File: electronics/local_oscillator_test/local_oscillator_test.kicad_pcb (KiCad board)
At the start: 2 copper layers, 0 parts

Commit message: Import works
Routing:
- removed copper zone on F.Cu, net (none)
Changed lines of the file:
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@@
     (visible_elements FFFFFF7F)
     (pcbplotparams
-      (layerselection 0x010fc_ffffffff)
+      (layerselection 0x00000_7fffffff)
       (usegerberextensions false)
       (usegerberattributes false)
@@
       (psnegative false)
       (psa4output false)
-      (plotreference true)
-      (plotvalue true)
+      (plotreference false)
+      (plotvalue false)
       (plotinvisibletext false)
       (padsonsilk false)
       (subtractmaskfromsilk false)
-      (outputformat 1)
+      (outputformat 4)
       (mirror false)
-      (drillshape 1)
+      (drillshape 0)
       (scaleselection 1)
       (outputdirectory ""))
@@
     (uvia_drill 0.1)
   )
-  (zone (net 0) (net_name "") (layer F.Cu) (hatch edge 0.508)
-    (connect_pads (clearance 0.508))
-    (min_thickness 0.254)
-    (fill yes (arc_segments 16) (thermal_gap 0.508) (thermal_bridge_width 0.508))
-    (polygon
-      (pts
-        (xy 100 45) (xy 110 45) (xy 110 55) (xy 100 55)
-      )
-    )
-  )
 )

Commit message: Modelled reference oscillator, gprMax impulse model is looking fine
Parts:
- added C1: 1pF, 0402, F.Cu at (18.4, 20.0)
- added U1: CE3520K3, 0xDBFB7:4-Micro-X, F.Cu at (22.4, 20.0)
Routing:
- net (no net): track 0.00 -> 55.0 mm
- net GND: track 0.00 -> 2.75 mm
- net /OSC1: track 0.00 -> 2.75 mm
- net /GATE: track 0.00 -> 2.75 mm
- added copper zone on F.Cu, net /GATE
- added copper zone on F.Cu, net /OSC1
- added copper zone on F.Cu, net GND
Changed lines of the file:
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@@
     (thickness 1.6)
     (drawings 0)
-    (tracks 0)
+    (tracks 8)
     (zones 0)
-    (modules 0)
-    (nets 1)
+    (modules 2)
+    (nets 4)
   )
   (page A4)
@@
     (last_trace_width 0.25)
     (trace_clearance 0.2)
-    (zone_clearance 0.508)
+    (zone_clearance 0)
     (zone_45_only no)
     (trace_min 0.2)
@@
     (pad_drill 0.762)
     (pad_to_mask_clearance 0.2)
-    (aux_axis_origin 0 0)
-    (visible_elements FFFFFF7F)
+    (aux_axis_origin 22.5 25)
+    (grid_origin 22.5 25)
+    (visible_elements FEFFFF7F)
     (pcbplotparams
       (layerselection 0x00000_7fffffff)
@@
   )
   (net 0 "")
+  (net 1 /OSC1)
+  (net 2 GND)
+  (net 3 /GATE)
   (net_class Default "This is the default net class."
     (clearance 0.2)
@@
     (uvia_dia 0.3)
     (uvia_drill 0.1)
+    (add_net /GATE)
+    (add_net /OSC1)
+    (add_net GND)
+  )
+  (module 0402 (layer F.Cu)
+    (at 18.35 20 90)
+    (descr "GENERIC 1005 (0402) PACKAGE")
+    (tags "GENERIC 1005 (0402) PACKAGE")
+    (attr smd)
+    (fp_text reference C1 (at 0 -1.27 90) (layer F.SilkS)
+      (effects (font (size 0.6096 0.6096) (thickness 0.127)))
+    )
+    (fp_text value 1pF (at 0 1.27 90) (layer F.SilkS)
+      (effects (font (size 0.6096 0.6096) (thickness 0.127)))
+    )
+    (fp_line (start -0.55372 0.3048) (end -0.254 0.3048) (layer Dwgs.User) (width 0.06604))
+    (fp_line (start -0.254 0.3048) (end -0.254 -0.3048) (layer Dwgs.User) (width 0.06604))
+    (fp_line (start -0.55372 -0.3048) (end -0.254 -0.3048) (layer Dwgs.User) (width 0.06604))
+    (fp_line (start -0.55372 0.3048) (end -0.55372 -0.3048) (layer Dwgs.User) (width 0.06604))
+    (fp_line (start 0.25654 0.3048) (end 0.5588 0.3048) (layer Dwgs.User) (width 0.06604))
+    (fp_line (start 0.5588 0.3048) (end 0.5588 -0.3048) (layer Dwgs.User) (width 0.06604))
+    (fp_line (start 0.25654 -0.3048) (end 0.5588 -0.3048) (layer Dwgs.User) (width 0.06604))
+    (fp_line (start 0.25654 0.3048) (end 0.25654 -0.3048) (layer Dwgs.User) (width 0.06604))
+    (fp_line (start -0.19812 0.29972) (end 0.19812 0.29972) (layer F.SilkS) (width 0.06604))
+    (fp_line (start 0.19812 0.29972) (end 0.19812 -0.29972) (layer F.SilkS) (width 0.06604))
+    (fp_line (start -0.19812 -0.29972) (end 0.19812 -0.29972) (layer F.SilkS) (width 0.06604))
+    (fp_line (start -0.19812 0.29972) (end -0.19812 -0.29972) (layer F.SilkS) (width 0.06604))
+    (fp_line (start -0.26924 -0.2286) (end 0.26924 -0.2286) (layer Dwgs.User) (width 0.1524))
+    (fp_line (start 0.26924 0.2286) (end -0.26924 0.2286) (layer Dwgs.User) (width 0.1524))
+    (fp_line (start -1.19888 -0.6477) (end 1.19888 -0.6477) (layer F.CrtYd) (width 0.0508))
+    (fp_line (start 1.19888 -0.6477) (end 1.19888 0.6477) (layer F.CrtYd) (width 0.0508))
+    (fp_line (start 1.19888 0.6477) (end -1.19888 0.6477) (layer F.CrtYd) (width 0.0508))
+    (fp_line (start -1.19888 0.6477) (end -1.19888 -0.6477) (layer F.CrtYd) (width 0.0508))
+    (pad 1 smd rect (at -0.57912 0 90) (size 0.84836 0.89916) (layers F.Cu F.Paste F.Mask)
+      (net 3 /GATE) (solder_mask_margin 0.1016))
+    (pad 2 smd rect (at 0.57912 0 90) (size 0.84836 0.89916) (layers F.Cu F.Paste F.Mask)
+      (net 1 /OSC1) (solder_mask_margin 0.1016))
+  )
+  (module 0xDBFB7:4-Micro-X (layer F.Cu)
+    (at 22.45 20 270)
+    (fp_text reference U1 (at 0 5.072 270) (layer F.SilkS)
+      (effects (font (size 1 1) (thickness 0.15)))
+    )
+    (fp_text value CE3520K3 (at 0 4.072 270) (layer F.Fab)
+      (effects (font (size 1 1) (thickness 0.15)))
+    )
+    (fp_text user Gate (at 1.4 -0.5 270) (layer Dwgs.User)
+      (effects (font (size 0.2 0.2) (thickness 0.05)))
+    )
+    (fp_text user Drain (at -1.3 -0.5 270) (layer Dwgs.User)
+      (effects (font (size 0.2 0.2) (thickness 0.05)))
+    )
+    (fp_text user Source (at -0.5 -1.3) (layer Dwgs.User)
+      (effects (font (size 0.2 0.2) (thickness 0.05)))
+    )
+    (fp_text user Source (at -0.5 1.4) (layer Dwgs.User)
+      (effects (font (size 0.2 0.2) (thickness 0.05)))
+    )
+    (fp_circle (center 0 0) (end 0.583095 0) (layer F.SilkS) (width 0.15))
+    (fp_circle (center 0.4 0) (end 0.5 0) (layer F.SilkS) (width 0.15))
+    (pad 2 smd rect (at -1.35 0) (size 0.65 1) (layers F.Cu F.Paste F.Mask)
+      (net 1 /OSC1))
+    (pad 1 smd rect (at 0 -1.35 270) (size 0.65 1) (layers F.Cu F.Paste F.Mask)
+      (net 2 GND))
+    (pad 4 smd rect (at 1.35 0 180) (size 0.65 1) (layers F.Cu F.Paste F.Mask)
+      (net 3 /GATE))
+    (pad 3 smd rect (at 0 1.35 90) (size 0.65 1) (layers F.Cu F.Paste F.Mask)
+      (net 2 GND))
+  )
+  (segment (start 27.5 27.5) (end 27.5 12.5) (width 0.25) (layer F.Cu) (net 0))
+  (segment (start 15 12.5) (end 15 27.5) (width 0.25) (layer F.Cu) (net 0))
+  (segment (start 15 27.5) (end 27.5 27.5) (width 0.25) (layer F.Cu) (net 0))
+  (segment (start 15 12.5) (end 27.25 12.5) (width 0.25) (layer F.Cu) (net 0))
+  (segment (start 27.25 12.5) (end 27.5 12.5) (width 0.25) (layer F.Cu) (net 0))
+  (segment (start 26.95 20) (end 24.2 20) (width 0.1) (layer F.Cu) (net 2))
+  (segment (start 22.45 22.5) (end 22.45 25.25) (width 0.1) (layer F.Cu) (net 3))
+  (segment (start 22.45 14.75) (end 22.45 17.5) (width 0.1) (layer F.Cu) (net 1))
+  (zone (net 3) (net_name /GATE) (layer F.Cu) (hatch edge 0.508)
+    (connect_pads yes (clearance 0.508))
+    (min_thickness 0.254)
+    (fill yes (arc_segments 16) (thermal_gap 0.508) (thermal_bridge_width 0.508))
+    (polygon
+      (pts
+        (xy 24.95 22.5) (xy 24.95 21) (xy 19.95 21) (xy 19.95 22.5)
+      )
+    )
+  )
+  (zone (net 1) (net_name /OSC1) (layer F.Cu) (hatch edge 0.508)
+    (connect_pads yes (clearance 0.508))
+    (min_thickness 0.254)
+    (fill yes (arc_segments 16) (thermal_gap 0.508) (thermal_bridge_width 0.508))
+    (polygon
+      (pts
+        (xy 24.95 19) (xy 24.95 17.5) (xy 19.95 17.5) (xy 19.95 19)
+      )
+    )
+  )
+  (zone (net 2) (net_name GND) (layer F.Cu) (hatch edge 0.508)
+    (connect_pads yes (clearance 0))
+    (min_thickness 0.254)
+    (fill yes (arc_segments 16) (thermal_gap 0) (thermal_bridge_width 0))
+    (polygon
+      (pts
+        (xy 19.95 19.75) (xy 24.95 19.75) (xy 24.95 20.25) (xy 19.95 20.25)
+      )
+    )
+  )
+  (zone (net 1) (net_name /OSC1) (layer F.Cu) (hatch edge 0.508)
+    (connect_pads yes (clearance 0))
+    (min_thickness 0.254)
+    (fill yes (arc_segments 16) (thermal_gap 0) (thermal_bridge_width 0))
+    (polygon
+      (pts
+        (xy 20.45 18) (xy 20.45 16.5) (xy 19.95 16.5) (xy 19.95 18)
+      )
+    )
+  )
+  (zone (net 1) (net_name /OSC1) (layer F.Cu) (hatch edge 0.508)
+    (connect_pads yes (clearance 0))
+    (min_thickness 0.254)
+    (fill yes (arc_segments 16) (thermal_gap 0) (thermal_bridge_width 0))
+    (polygon
+      (pts
+        (xy 20.45 16.5) (xy 20.45 17.25) (xy 17.95 17.25) (xy 17.95 16.5)
+      )
+    )
+  )
+  (zone (net 1) (net_name /OSC1) (layer F.Cu) (hatch edge 0.508)
+    (connect_pads yes (clearance 0))
+    (min_thickness 0.254)
+    (fill yes (arc_segments 16) (thermal_gap 0) (thermal_bridge_width 0))
+    (polygon
+      (pts
+        (xy 17.95 16.5) (xy 17.95 19.5) (xy 18.7 19.5) (xy 18.7 16.5)
+      )
+    )
+  )
+  (zone (net 3) (net_name /GATE) (layer F.Cu) (hatch edge 0.508)
+    (connect_pads yes (clearance 0))
+    (min_thickness 0.254)
+    (fill yes (arc_segments 16) (thermal_gap 0) (thermal_bridge_width 0))
+    (polygon
+      (pts
+        (xy 20.45 22) (xy 20.45 23.5) (xy 19.95 23.5) (xy 19.95 22)
+      )
+    )
+  )
+  (zone (net 3) (net_name /GATE) (layer F.Cu) (hatch edge 0.508)
+    (connect_pads yes (clearance 0))
+    (min_thickness 0.254)
+    (fill yes (arc_segments 16) (thermal_gap 0) (thermal_bridge_width 0))
+    (polygon
+      (pts
+        (xy 20.45 23.5) (xy 17.95 23.5) (xy 17.95 20.5) (xy 18.7 20.5) (xy 18.7 22.75)
+        (xy 20.45 22.75)
+      )
+    )
   )
 )

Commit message: Something resembling an impulse
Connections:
- C1 pad 2: /OSC1 -> /GATE
- U1 pad 2: /OSC1 -> /GATE
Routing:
- net (no net): track 55.0 -> 1.00 mm
- net /GATE: track 2.75 -> 3.91 mm
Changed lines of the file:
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@@
       (net 3 /GATE) (solder_mask_margin 0.1016))
     (pad 2 smd rect (at 0.57912 0 90) (size 0.84836 0.89916) (layers F.Cu F.Paste F.Mask)
-      (net 1 /OSC1) (solder_mask_margin 0.1016))
+      (net 3 /GATE) (solder_mask_margin 0.1016))
   )
   (module 0xDBFB7:4-Micro-X (layer F.Cu)
@@
     (fp_circle (center 0.4 0) (end 0.5 0) (layer F.SilkS) (width 0.15))
     (pad 2 smd rect (at -1.35 0) (size 0.65 1) (layers F.Cu F.Paste F.Mask)
-      (net 1 /OSC1))
+      (net 3 /GATE))
     (pad 1 smd rect (at 0 -1.35 270) (size 0.65 1) (layers F.Cu F.Paste F.Mask)
       (net 2 GND))
@@
       (net 2 GND))
   )
-  (segment (start 27.5 27.5) (end 27.5 12.5) (width 0.25) (layer F.Cu) (net 0))
-  (segment (start 15 12.5) (end 15 27.5) (width 0.25) (layer F.Cu) (net 0))
-  (segment (start 15 27.5) (end 27.5 27.5) (width 0.25) (layer F.Cu) (net 0))
-  (segment (start 15 12.5) (end 27.25 12.5) (width 0.25) (layer F.Cu) (net 0))
-  (segment (start 27.25 12.5) (end 27.5 12.5) (width 0.25) (layer F.Cu) (net 0))
+  (segment (start 15 12.75) (end 15 12.5) (width 0.05) (layer F.Cu) (net 0))
+  (segment (start 15 12.5) (end 15.25 12.5) (width 0.05) (layer F.Cu) (net 0))
+  (segment (start 28.75 27.25) (end 28.75 27.5) (width 0.05) (layer F.Cu) (net 0))
+  (segment (start 28.75 27.5) (end 28.5 27.5) (width 0.05) (layer F.Cu) (net 0))
   (segment (start 26.95 20) (end 24.2 20) (width 0.1) (layer F.Cu) (net 2))
   (segment (start 22.45 22.5) (end 22.45 25.25) (width 0.1) (layer F.Cu) (net 3))
   (segment (start 22.45 14.75) (end 22.45 17.5) (width 0.1) (layer F.Cu) (net 1))
+  (segment (start 18.35 19.42088) (end 18.35 20.57912) (width 0.5) (layer F.Cu) (net 3))
   (zone (net 3) (net_name /GATE) (layer F.Cu) (hatch edge 0.508)
     (connect_pads yes (clearance 0.508))
@@
     )
   )
-  (zone (net 1) (net_name /OSC1) (layer F.Cu) (hatch edge 0.508)
+  (zone (net 3) (net_name /GATE) (layer F.Cu) (hatch edge 0.508)
     (connect_pads yes (clearance 0.508))
     (min_thickness 0.254)
@@
     )
   )
-  (zone (net 1) (net_name /OSC1) (layer F.Cu) (hatch edge 0.508)
+  (zone (net 3) (net_name /GATE) (layer F.Cu) (hatch edge 0.508)
     (connect_pads yes (clearance 0))
     (min_thickness 0.254)
@@
       )
     )
+  )
+  (zone (net 1) (net_name /OSC1) (layer F.Cu) (hatch edge 0.508)
+    (connect_pads yes (clearance 0))
+    (min_thickness 0.254)
+    (fill yes (arc_segments 16) (thermal_gap 0) (thermal_bridge_width 0))
+    (polygon
+      (pts
+        (xy 22 15) (xy 23 15) (xy 23 14) (xy 22 14)
+      )
+    )
+  )
+  (zone (net 2) (net_name GND) (layer F.Cu) (hatch edge 0.508)
+    (connect_pads yes (clearance 0))
+    (min_thickness 0.254)
+    (fill yes (arc_segments 16) (thermal_gap 0) (thermal_bridge_width 0))
+    (polygon
+      (pts
+        (xy 26.75 19.5) (xy 26.75 20.5) (xy 27.75 20.5) (xy 27.75 19.5)
+      )
+    )
+  )
+  (zone (net 3) (net_name /GATE) (layer F.Cu) (hatch edge 0.508)
+    (connect_pads yes (clearance 0))
+    (min_thickness 0.254)
+    (fill yes (arc_segments 16) (thermal_gap 0) (thermal_bridge_width 0))
+    (polygon
+      (pts
+        (xy 23 25) (xy 22 25) (xy 22 26) (xy 23 26)
+      )
+    )

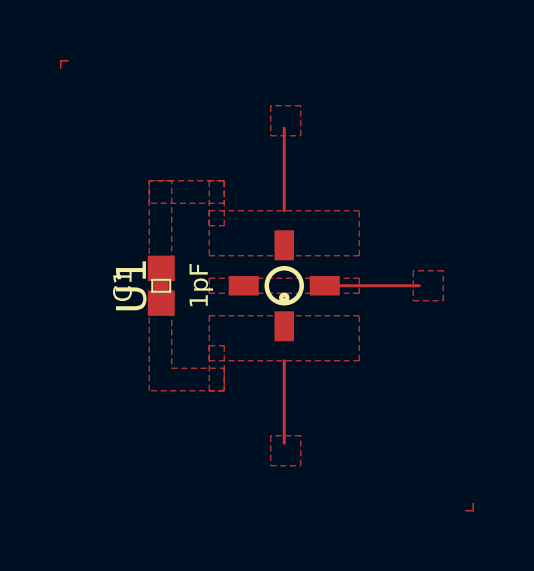
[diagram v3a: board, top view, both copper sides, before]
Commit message: Trying a simple microstrip
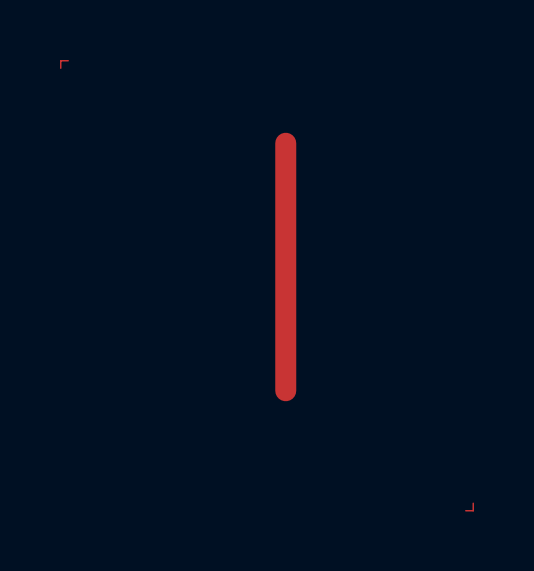
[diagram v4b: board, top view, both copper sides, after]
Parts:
- removed C1: 1pF, 0402
- removed U1: CE3520K3, 0xDBFB7:4-Micro-X
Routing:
- net (no net): track 1.00 -> 9.25 mm
- net /GATE: track 3.91 -> 0.00 mm
- net GND: track 2.75 -> 0.00 mm
- net /OSC1: track 2.75 -> 0.00 mm
- removed copper zone on F.Cu, net /GATE
- removed copper zone on F.Cu, net /OSC1
- removed copper zone on F.Cu, net GND
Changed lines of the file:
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@@
     (thickness 1.6)
     (drawings 0)
-    (tracks 8)
+    (tracks 5)
     (zones 0)
-    (modules 2)
-    (nets 4)
+    (modules 0)
+    (nets 1)
   )
   (page A4)
@@
   )
   (net 0 "")
-  (net 1 /OSC1)
-  (net 2 GND)
-  (net 3 /GATE)
   (net_class Default "This is the default net class."
     (clearance 0.2)
@@
     (uvia_dia 0.3)
     (uvia_drill 0.1)
-    (add_net /GATE)
-    (add_net /OSC1)
-    (add_net GND)
-  )
-  (module 0402 (layer F.Cu)
-    (at 18.35 20 90)
-    (descr "GENERIC 1005 (0402) PACKAGE")
-    (tags "GENERIC 1005 (0402) PACKAGE")
-    (attr smd)
-    (fp_text reference C1 (at 0 -1.27 90) (layer F.SilkS)
-      (effects (font (size 0.6096 0.6096) (thickness 0.127)))
-    )
-    (fp_text value 1pF (at 0 1.27 90) (layer F.SilkS)
-      (effects (font (size 0.6096 0.6096) (thickness 0.127)))
-    )
-    (fp_line (start -0.55372 0.3048) (end -0.254 0.3048) (layer Dwgs.User) (width 0.06604))
-    (fp_line (start -0.254 0.3048) (end -0.254 -0.3048) (layer Dwgs.User) (width 0.06604))
-    (fp_line (start -0.55372 -0.3048) (end -0.254 -0.3048) (layer Dwgs.User) (width 0.06604))
-    (fp_line (start -0.55372 0.3048) (end -0.55372 -0.3048) (layer Dwgs.User) (width 0.06604))
-    (fp_line (start 0.25654 0.3048) (end 0.5588 0.3048) (layer Dwgs.User) (width 0.06604))
-    (fp_line (start 0.5588 0.3048) (end 0.5588 -0.3048) (layer Dwgs.User) (width 0.06604))
-    (fp_line (start 0.25654 -0.3048) (end 0.5588 -0.3048) (layer Dwgs.User) (width 0.06604))
-    (fp_line (start 0.25654 0.3048) (end 0.25654 -0.3048) (layer Dwgs.User) (width 0.06604))
-    (fp_line (start -0.19812 0.29972) (end 0.19812 0.29972) (layer F.SilkS) (width 0.06604))
-    (fp_line (start 0.19812 0.29972) (end 0.19812 -0.29972) (layer F.SilkS) (width 0.06604))
-    (fp_line (start -0.19812 -0.29972) (end 0.19812 -0.29972) (layer F.SilkS) (width 0.06604))
-    (fp_line (start -0.19812 0.29972) (end -0.19812 -0.29972) (layer F.SilkS) (width 0.06604))
-    (fp_line (start -0.26924 -0.2286) (end 0.26924 -0.2286) (layer Dwgs.User) (width 0.1524))
-    (fp_line (start 0.26924 0.2286) (end -0.26924 0.2286) (layer Dwgs.User) (width 0.1524))
-    (fp_line (start -1.19888 -0.6477) (end 1.19888 -0.6477) (layer F.CrtYd) (width 0.0508))
-    (fp_line (start 1.19888 -0.6477) (end 1.19888 0.6477) (layer F.CrtYd) (width 0.0508))
-    (fp_line (start 1.19888 0.6477) (end -1.19888 0.6477) (layer F.CrtYd) (width 0.0508))
-    (fp_line (start -1.19888 0.6477) (end -1.19888 -0.6477) (layer F.CrtYd) (width 0.0508))
-    (pad 1 smd rect (at -0.57912 0 90) (size 0.84836 0.89916) (layers F.Cu F.Paste F.Mask)
-      (net 3 /GATE) (solder_mask_margin 0.1016))
-    (pad 2 smd rect (at 0.57912 0 90) (size 0.84836 0.89916) (layers F.Cu F.Paste F.Mask)
-      (net 3 /GATE) (solder_mask_margin 0.1016))
-  )
-  (module 0xDBFB7:4-Micro-X (layer F.Cu)
-    (at 22.45 20 270)
-    (fp_text reference U1 (at 0 5.072 270) (layer F.SilkS)
-      (effects (font (size 1 1) (thickness 0.15)))
-    )
-    (fp_text value CE3520K3 (at 0 4.072 270) (layer F.Fab)
-      (effects (font (size 1 1) (thickness 0.15)))
-    )
-    (fp_text user Gate (at 1.4 -0.5 270) (layer Dwgs.User)
-      (effects (font (size 0.2 0.2) (thickness 0.05)))
-    )
-    (fp_text user Drain (at -1.3 -0.5 270) (layer Dwgs.User)
-      (effects (font (size 0.2 0.2) (thickness 0.05)))
-    )
-    (fp_text user Source (at -0.5 -1.3) (layer Dwgs.User)
-      (effects (font (size 0.2 0.2) (thickness 0.05)))
-    )
-    (fp_text user Source (at -0.5 1.4) (layer Dwgs.User)
-      (effects (font (size 0.2 0.2) (thickness 0.05)))
-    )
-    (fp_circle (center 0 0) (end 0.583095 0) (layer F.SilkS) (width 0.15))
-    (fp_circle (center 0.4 0) (end 0.5 0) (layer F.SilkS) (width 0.15))
-    (pad 2 smd rect (at -1.35 0) (size 0.65 1) (layers F.Cu F.Paste F.Mask)
-      (net 3 /GATE))
-    (pad 1 smd rect (at 0 -1.35 270) (size 0.65 1) (layers F.Cu F.Paste F.Mask)
-      (net 2 GND))
-    (pad 4 smd rect (at 1.35 0 180) (size 0.65 1) (layers F.Cu F.Paste F.Mask)
-      (net 3 /GATE))
-    (pad 3 smd rect (at 0 1.35 90) (size 0.65 1) (layers F.Cu F.Paste F.Mask)
-      (net 2 GND))
   )
   (segment (start 15 12.75) (end 15 12.5) (width 0.05) (layer F.Cu) (net 0))
@@
   (segment (start 28.75 27.25) (end 28.75 27.5) (width 0.05) (layer F.Cu) (net 0))
   (segment (start 28.75 27.5) (end 28.5 27.5) (width 0.05) (layer F.Cu) (net 0))
-  (segment (start 26.95 20) (end 24.2 20) (width 0.1) (layer F.Cu) (net 2))
-  (segment (start 22.45 22.5) (end 22.45 25.25) (width 0.1) (layer F.Cu) (net 3))
-  (segment (start 22.45 14.75) (end 22.45 17.5) (width 0.1) (layer F.Cu) (net 1))
-  (segment (start 18.35 19.42088) (end 18.35 20.57912) (width 0.5) (layer F.Cu) (net 3))
-  (zone (net 3) (net_name /GATE) (layer F.Cu) (hatch edge 0.508)
-    (connect_pads yes (clearance 0.508))
-    (min_thickness 0.254)
-    (fill yes (arc_segments 16) (thermal_gap 0.508) (thermal_bridge_width 0.508))
-    (polygon
-      (pts
-        (xy 24.95 22.5) (xy 24.95 21) (xy 19.95 21) (xy 19.95 22.5)
-      )
-    )
-  )
-  (zone (net 3) (net_name /GATE) (layer F.Cu) (hatch edge 0.508)
-    (connect_pads yes (clearance 0.508))
-    (min_thickness 0.254)
-    (fill yes (arc_segments 16) (thermal_gap 0.508) (thermal_bridge_width 0.508))
-    (polygon
-      (pts
-        (xy 24.95 19) (xy 24.95 17.5) (xy 19.95 17.5) (xy 19.95 19)
-      )
-    )
-  )
-  (zone (net 2) (net_name GND) (layer F.Cu) (hatch edge 0.508)
-    (connect_pads yes (clearance 0))
-    (min_thickness 0.254)
-    (fill yes (arc_segments 16) (thermal_gap 0) (thermal_bridge_width 0))
-    (polygon
-      (pts
-        (xy 19.95 19.75) (xy 24.95 19.75) (xy 24.95 20.25) (xy 19.95 20.25)
-      )
-    )
-  )
-  (zone (net 1) (net_name /OSC1) (layer F.Cu) (hatch edge 0.508)
-    (connect_pads yes (clearance 0))
-    (min_thickness 0.254)
-    (fill yes (arc_segments 16) (thermal_gap 0) (thermal_bridge_width 0))
-    (polygon
-      (pts
-        (xy 20.45 18) (xy 20.45 16.5) (xy 19.95 16.5) (xy 19.95 18)
-      )
-    )
-  )
-  (zone (net 1) (net_name /OSC1) (layer F.Cu) (hatch edge 0.508)
-    (connect_pads yes (clearance 0))
-    (min_thickness 0.254)
-    (fill yes (arc_segments 16) (thermal_gap 0) (thermal_bridge_width 0))
-    (polygon
-      (pts
-        (xy 20.45 16.5) (xy 20.45 17.25) (xy 17.95 17.25) (xy 17.95 16.5)
-      )
-    )
-  )
-  (zone (net 3) (net_name /GATE) (layer F.Cu) (hatch edge 0.508)
-    (connect_pads yes (clearance 0))
-    (min_thickness 0.254)
-    (fill yes (arc_segments 16) (thermal_gap 0) (thermal_bridge_width 0))
-    (polygon
-      (pts
-        (xy 17.95 16.5) (xy 17.95 19.5) (xy 18.7 19.5) (xy 18.7 16.5)
-      )
-    )
-  )
-  (zone (net 3) (net_name /GATE) (layer F.Cu) (hatch edge 0.508)
-    (connect_pads yes (clearance 0))
-    (min_thickness 0.254)
-    (fill yes (arc_segments 16) (thermal_gap 0) (thermal_bridge_width 0))
-    (polygon
-      (pts
-        (xy 20.45 22) (xy 20.45 23.5) (xy 19.95 23.5) (xy 19.95 22)
-      )
-    )
-  )
-  (zone (net 3) (net_name /GATE) (layer F.Cu) (hatch edge 0.508)
-    (connect_pads yes (clearance 0))
-    (min_thickness 0.254)
-    (fill yes (arc_segments 16) (thermal_gap 0) (thermal_bridge_width 0))
-    (polygon
-      (pts
-        (xy 20.45 23.5) (xy 17.95 23.5) (xy 17.95 20.5) (xy 18.7 20.5) (xy 18.7 22.75)
-        (xy 20.45 22.75)
-      )
-    )
-  )
-  (zone (net 1) (net_name /OSC1) (layer F.Cu) (hatch edge 0.508)
-    (connect_pads yes (clearance 0))
-    (min_thickness 0.254)
-    (fill yes (arc_segments 16) (thermal_gap 0) (thermal_bridge_width 0))
-    (polygon
-      (pts
-        (xy 22 15) (xy 23 15) (xy 23 14) (xy 22 14)
-      )
-    )
-  )
-  (zone (net 2) (net_name GND) (layer F.Cu) (hatch edge 0.508)
-    (connect_pads yes (clearance 0))
-    (min_thickness 0.254)
-    (fill yes (arc_segments 16) (thermal_gap 0) (thermal_bridge_width 0))
-    (polygon
-      (pts
-        (xy 26.75 19.5) (xy 26.75 20.5) (xy 27.75 20.5) (xy 27.75 19.5)
-      )
-    )
-  )
-  (zone (net 3) (net_name /GATE) (layer F.Cu) (hatch edge 0.508)
-    (connect_pads yes (clearance 0))
-    (min_thickness 0.254)
-    (fill yes (arc_segments 16) (thermal_gap 0) (thermal_bridge_width 0))
-    (polygon
-      (pts
-        (xy 23 25) (xy 22 25) (xy 22 26) (xy 23 26)
-      )
-    )
-  )
+  (segment (start 22.5 15.25) (end 22.5 23.5) (width 0.7) (layer F.Cu) (net 0))
 )
